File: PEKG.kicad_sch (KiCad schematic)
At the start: 65 parts, among them J1 AudioJack4, J2 AudioJack3_SwitchTR, SW1 SW_DPDT_x2, U1 OP07, U3 OP07, U4 NE5532, U5 NE5532

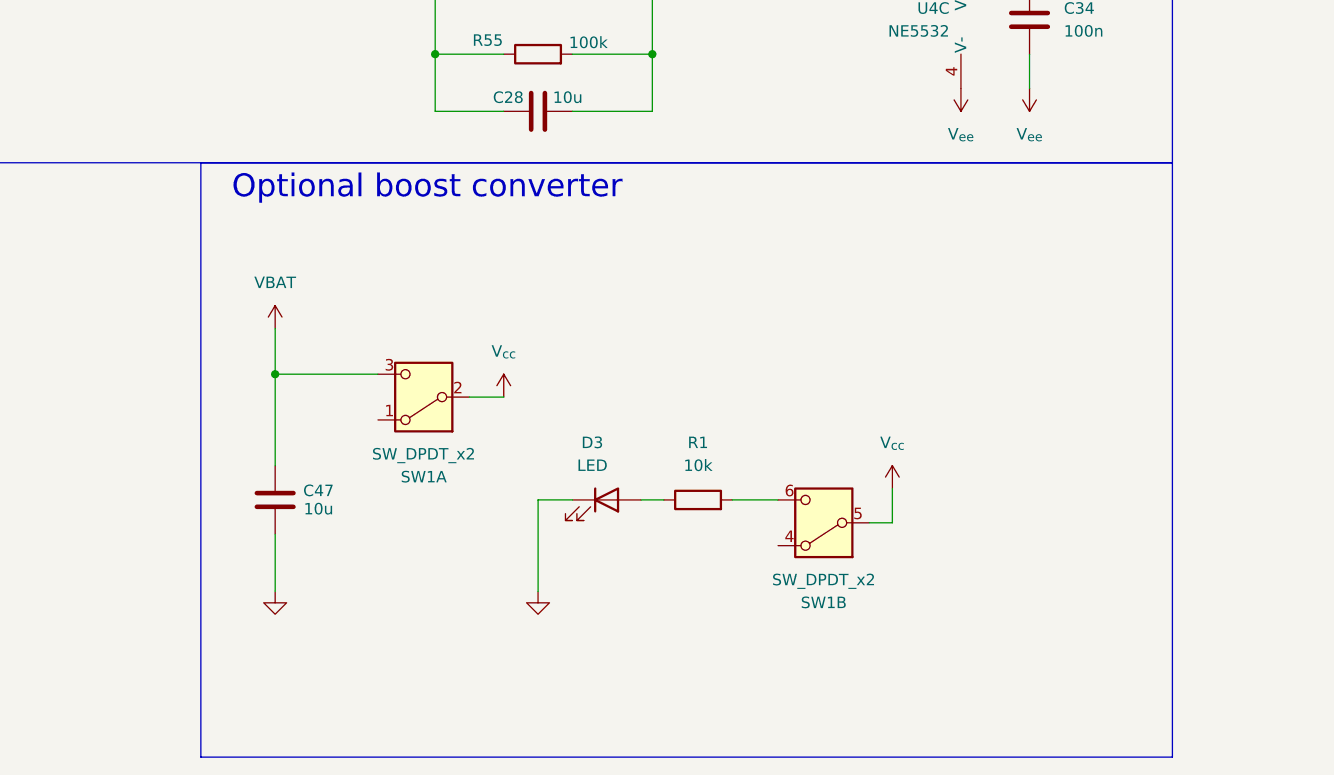
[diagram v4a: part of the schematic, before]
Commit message: updated form factor and placment
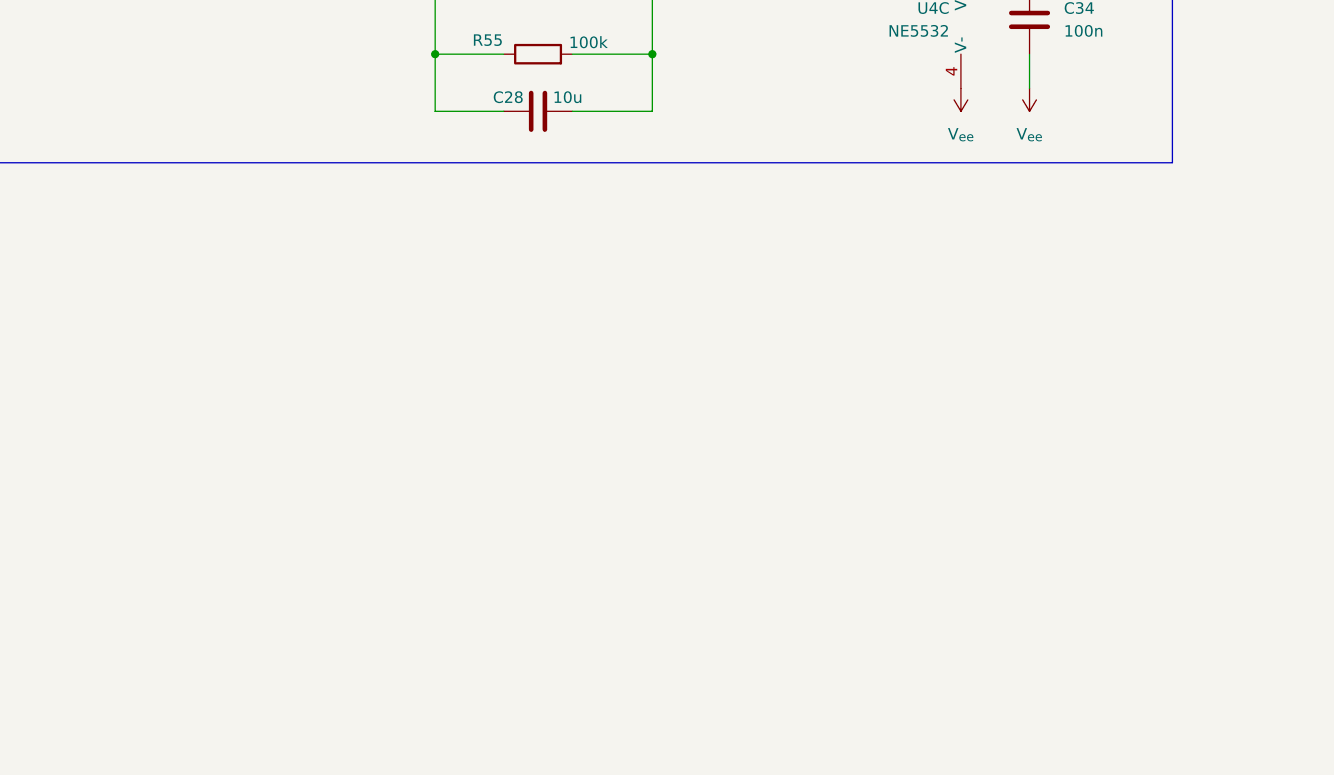
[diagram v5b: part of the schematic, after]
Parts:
- removed C47: 10u, Capacitor_SMD:C_0603_1608Metric_Pad1.08x0.95mm_HandSolder, symbol Device:C
- removed D3: LED, LED_SMD:LED_0603_1608Metric_Pad1.05x0.95mm_HandSolder, symbol Device:LED
- removed R1: 10k, Resistor_SMD:R_0603_1608Metric_Pad0.98x0.95mm_HandSolder, symbol Device:R
- removed SW1: SW_DPDT_x2, PEKG:DPDT_bigger, symbol Switch:SW_DPDT_x2
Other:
- note removed: "Optional boost converter"

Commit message: ADC, levels
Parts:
- removed C13, C15, C16, C25: 10n, Capacitor_SMD:C_0603_1608Metric_Pad1.08x0.95mm_HandSolder, symbol Device:C
- removed C26, C27, C28, C48: 10u, Capacitor_SMD:C_0603_1608Metric_Pad1.08x0.95mm_HandSolder, symbol Device:C
- removed C32, C33, C34, C44: 100n, Capacitor_SMD:C_0603_1608Metric_Pad1.08x0.95mm_HandSolder, symbol Device:C
- removed D1, D2: BAV99, Package_TO_SOT_SMD:SOT-23, symbol Diode:BAV99
- removed J1: AudioJack4, PEKG:Jack_3.5mm_4pole, symbol Connector_Audio:AudioJack4
- removed J2: AudioJack3_SwitchTR, PEKG:Jack_3.5mm_CUI_SJ1-3525N_Horizontal, symbol Connector_Audio:AudioJack3_SwitchTR
- removed JP3, JP9: Jumper_2_Bridged, Jumper:SolderJumper-2_P1.3mm_Bridged_RoundedPad1.0x1.5mm, symbol Jumper:Jumper_2_Bridged
- removed JP4: Jumper_2_Open, Jumper:SolderJumper-2_P1.3mm_Open_RoundedPad1.0x1.5mm, symbol Jumper:Jumper_2_Open
- removed R10, R11, R12, R26, R41, R44, R45, R46: 10k, Resistor_SMD:R_0603_1608Metric_Pad0.98x0.95mm_HandSolder, symbol Device:R
- removed R13: 1, Resistor_SMD:R_0603_1608Metric_Pad0.98x0.95mm_HandSolder, symbol Device:R
- removed R2: 100, Resistor_SMD:R_0603_1608Metric_Pad0.98x0.95mm_HandSolder, symbol Device:R
- removed R28, R29, R42, R43, R51, R53, R54, R55: 100k, Resistor_SMD:R_0603_1608Metric_Pad0.98x0.95mm_HandSolder, symbol Device:R
- removed R3, R4: 200k, Resistor_SMD:R_0603_1608Metric_Pad0.98x0.95mm_HandSolder, symbol Device:R
- removed R49, R50: 20k, Resistor_SMD:R_0603_1608Metric_Pad0.98x0.95mm_HandSolder, symbol Device:R
- removed R60: 1Meg, Resistor_SMD:R_0603_1608Metric_Pad0.98x0.95mm_HandSolder, symbol Device:R
- removed TP10, TP12, TP13, TP14, TP3, TP4, TP5, TP6, TP7, TP8, TP9: TestPoint, TestPoint:TestPoint_Pad_D3.0mm, symbol Connector:TestPoint
- removed U1, U3: OP07, Package_SO:SOIC-8_3.9x4.9mm_P1.27mm, symbol Amplifier_Operational:OP07
- removed U4: NE5532, symbol Amplifier_Operational:NE5532
- removed U5: NE5532, Package_SO:SOIC-8_3.9x4.9mm_P1.27mm, symbol Amplifier_Operational:NE5532
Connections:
- no-connect marks 4 -> 0
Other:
- added sheet Amplifier (amplifier.kicad_sch)
- sheet MCU ports: added +3V3, OUTPUT_ADC; removed none
- note removed: "10x gain"
- note removed: "ADD ON SWITCH"
- note removed: "DC component removal"
- note removed: "EKG differential input and leg drive"
- note removed: "Input body terminals"
- note removed: "Output connector"
- moved on the sheet: H1, H2, H3, H4
